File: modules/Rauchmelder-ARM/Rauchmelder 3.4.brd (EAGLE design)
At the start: 38 x 65 mm, 61 parts, among them IC2 LPC1115, IC3 BD9G101, Q1 BC856, Q3 BCP52, Q4 ASFL, T1 BC848

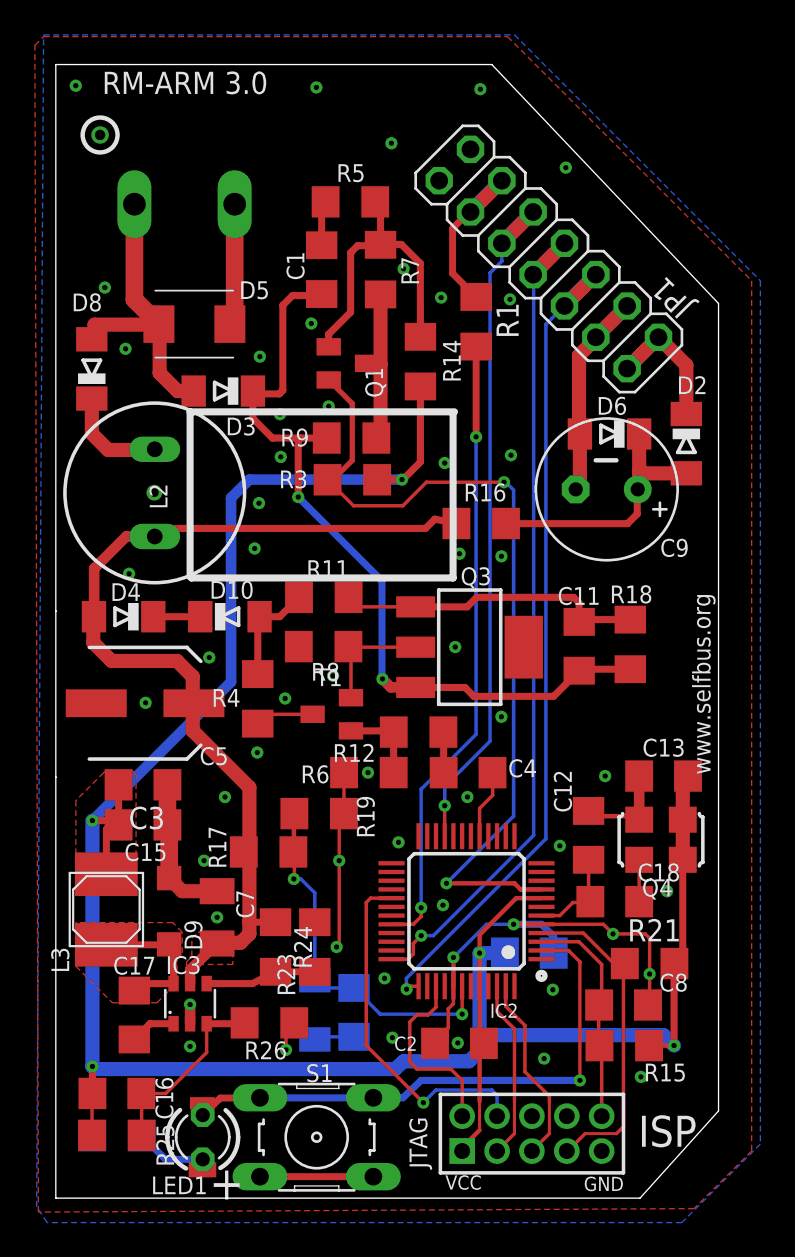
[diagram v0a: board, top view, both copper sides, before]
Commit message: silkscreen tvalue not printing on brd
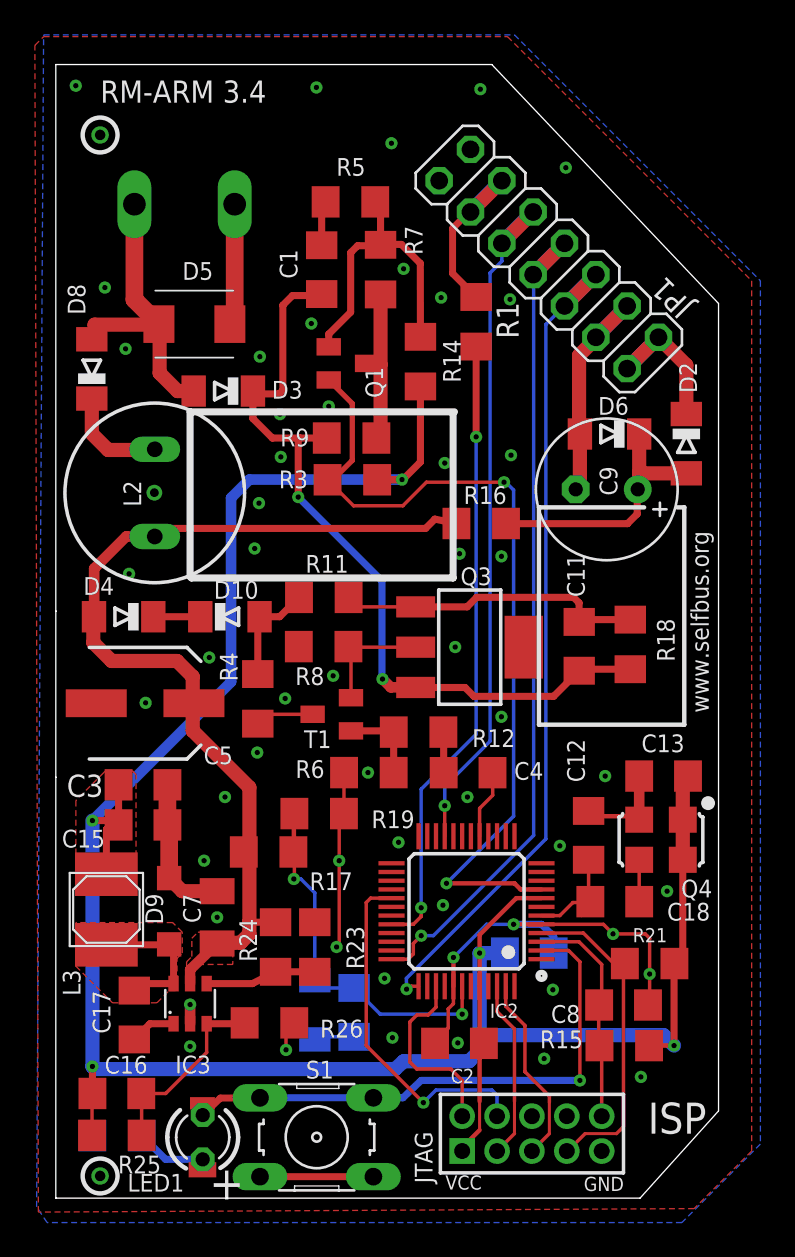
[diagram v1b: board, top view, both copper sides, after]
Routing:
- net GND: vias 56 -> 57
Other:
- board text added: "RM-ARM 3.4"
- board text removed: "RM-ARM 3.0"
